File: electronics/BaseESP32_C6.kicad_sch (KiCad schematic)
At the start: 14 parts, among them P4 CONN_01X09, SW1 SW_Push, U1 ESP32-C6-MINI-1/U

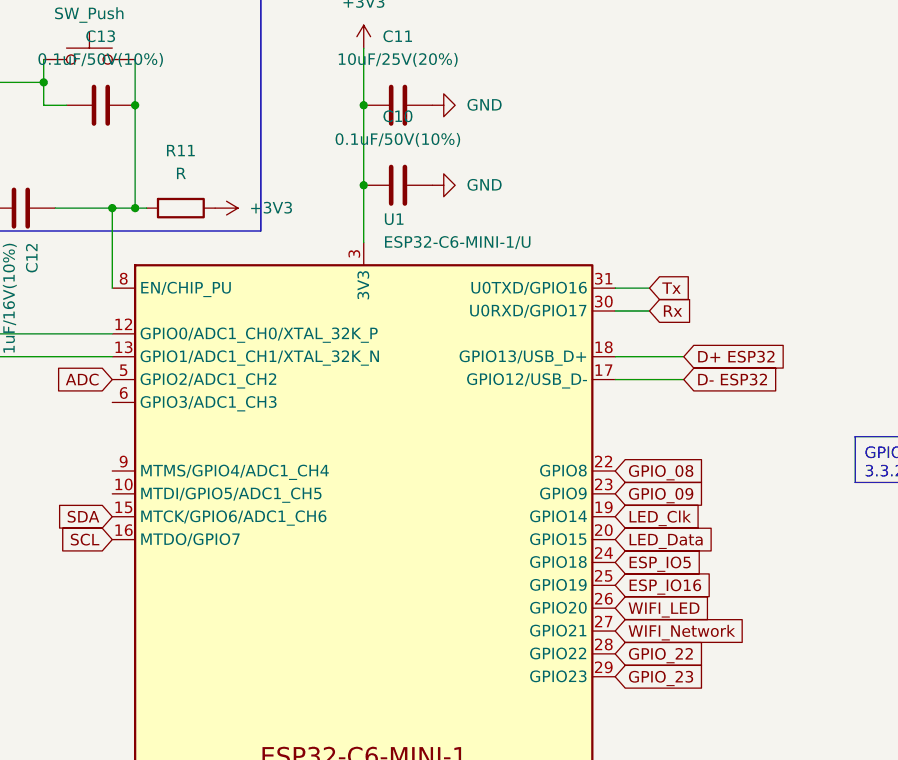
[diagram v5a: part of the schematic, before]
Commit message: Tidied tracks, added keepouts for ESP. Parts sourced except leds and small caps
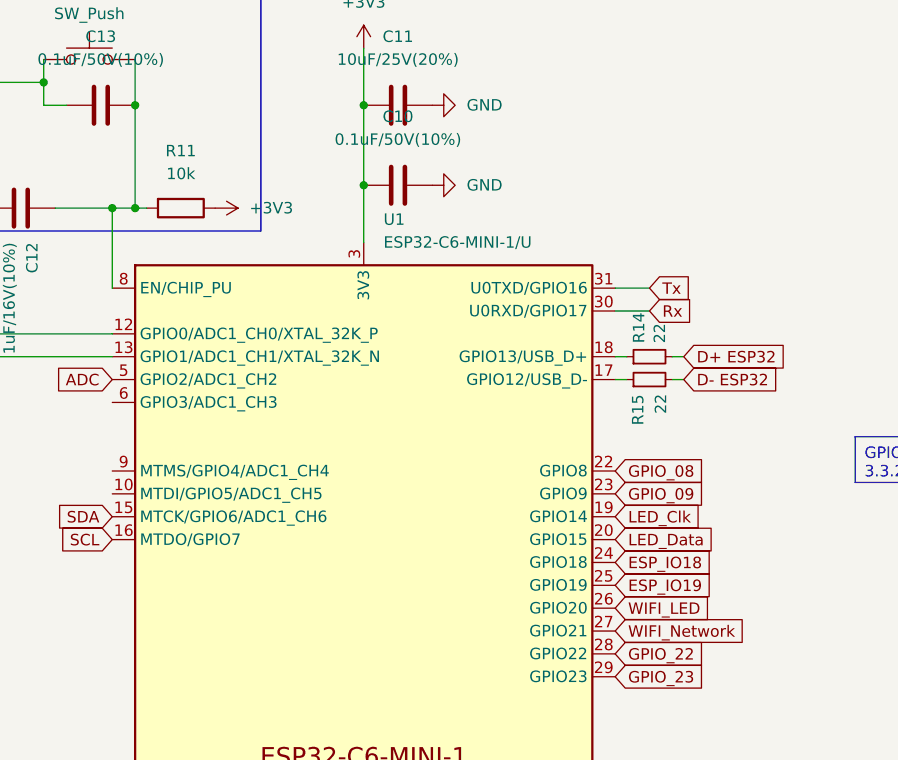
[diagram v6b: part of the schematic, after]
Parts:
- added R14, R15: 22, Resistor_SMD:R_0603_1608Metric_Pad0.98x0.95mm_HandSolder, symbol Device:R_Small
- R11: value R -> 10k; LCSC (none) -> C862388; LCSC Stock (none) -> https://www.lcsc.com/product-detail/Chip-span-style-backgro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
- R12, R13: LCSC (none) -> C5455512; LCSC Stock (none) -> https://www.lcsc.com/product-detail/Chip-span-style-backgro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
- U1: LCSC (none) -> C5736265; LCSC Stock (none) -> https://www.lcsc.com/product-detail/WiFi-Modules_Espressif-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
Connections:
- net D+ ESP32: now also R14.2; no longer U1.18 (GPIO13/USB_D+)
- net D- ESP32: now also R15.2; no longer U1.17 (GPIO12/USB_D-)
- net ESP_IO16 renamed ESP_IO19
- net ESP_IO5 renamed ESP_IO18
- new net: R14.1, U1.18 (GPIO13/USB_D+)
- new net: R15.1, U1.17 (GPIO12/USB_D-)
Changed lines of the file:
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@@
+    (stroke (width 0) (type default))
+  )
+  (wire (pts (xy 204.47 88.9) (xy 205.74 88.9))
     (stroke (width 0) (type default))
   )
@@
     (stroke (width 0) (type default))
   )
-  (wire (pts (xy 198.12 88.9) (xy 205.74 88.9))
-    (stroke (width 0) (type default))
-  )
   (wire (pts (xy 250.19 151.13) (xy 255.27 151.13))
     (stroke (width 0) (type default))
   )
+  (wire (pts (xy 198.12 88.9) (xy 199.39 88.9))
+    (stroke (width 0) (type default))
+  )
   (wire (pts (xy 134.62 60.96) (xy 134.62 58.42))
     (stroke (width 0) (type default))
@@
     (stroke (width 0) (type default))
   )
+  (wire (pts (xy 198.12 91.44) (xy 199.39 91.44))
+    (stroke (width 0) (type default))
+  )
   (wire (pts (xy 119.38 86.36) (xy 142.24 86.36))
     (stroke (width 0) (type default))
@@
     (stroke (width 0) (type default))
   )
-  (wire (pts (xy 198.12 91.44) (xy 205.74 91.44))
-    (stroke (width 0) (type default))
-  )
   (wire (pts (xy 135.89 72.39) (xy 142.24 72.39))
+    (stroke (width 0) (type default))
+  )
+  (wire (pts (xy 204.47 91.44) (xy 205.74 91.44))
     (stroke (width 0) (type default))
   )
@@
     )
   )
-  (global_label "ESP_IO5" (shape input) (at 198.12 111.76 0) (fields_autoplaced)
-    (effects (font (size 1.27 1.27)) (justify left))
-    (property "Intersheetrefs" "${INTERSHEET_REFS}" (at 207.9537 111.76 0)
+  (global_label "ESP_IO18" (shape input) (at 198.12 111.76 0) (fields_autoplaced)
+    (effects (font (size 1.27 1.27)) (justify left))
+    (property "Intersheetrefs" "${INTERSHEET_REFS}" (at 209.4014 111.76 0)
       (effects (font (size 1.27 1.27)) (justify left) hide)
     )
@@
     )
   )
-  (global_label "ESP_IO16" (shape input) (at 198.12 114.3 0) (fields_autoplaced)
-    (effects (font (size 1.27 1.27)) (justify left))
-    (property "Intersheetrefs" "${INTERSHEET_REFS}" (at 209.1632 114.3 0)
+  (global_label "ESP_IO19" (shape input) (at 198.12 114.3 0) (fields_autoplaced)
+    (effects (font (size 1.27 1.27)) (justify left))
+    (property "Intersheetrefs" "${INTERSHEET_REFS}" (at 209.4014 114.3 0)
       (effects (font (size 1.27 1.27)) (justify left) hide)
     )
@@
     )
   )
+  (symbol (lib_id "Device:R_Small") (at 201.93 88.9 90) (unit 1)
+    (in_bom yes) (on_board yes) (dnp no)
+    (property "Reference" "R14" (at 200.7616 87.4014 0)
+      (effects (font (size 1.27 1.27)) (justify left))
+    )
+    (property "Value" "22" (at 203.073 87.4014 0)
+      (effects (font (size 1.27 1.27)) (justify left))
+    )
+    (property "Footprint" "Resistor_SMD:R_0603_1608Metric_Pad0.98x0.95mm_HandSolder" (at 201.93 88.9 0)
+      (effects (font (size 1.27 1.27)) hide)
+    )
+    (property "Datasheet" "~" (at 201.93 88.9 0)
+      (effects (font (size 1.27 1.27)) hide)
+    )
+    (property "Farnell" "3495168 " (at 201.93 88.9 0)
+      (effects (font (size 1.27 1.27)) hide)
+    )
+    (property "Farnell Price/Stock" "https://uk.farnell.com/yageo/ac0201fr-0722rl/res-22r-1-0-05w-0201-thick-film/dp/3495168" (at 201.93 88.9 0)
+      (effects (font (size 1.27 1.27)) hide)
+    )
+    (property "LCSC" "C860239" (at 201.93 88.9 0)
+      (effects (font (size 1.27 1.27)) hide)
+    )
+    (property "LCSC Stock" "https://www.lcsc.com/product-detail/Chip-span-style-background-color-ff0-Resistor-span-Surface-Mount_YAGEO-RT0603BRB0722RL_C860239.html" (at 201.93 88.9 0)
+      (effects (font (size 1.27 1.27)) hide)
+    )
+    (pin "1")
+    (pin "2")
+    (instances
+      (project "MyBikesGotLED"
+        (path "/ea56fda8-6f8e-4826-a040-5c9b3e8e5cfa/88a3a1ef-5bc6-4f24-9217-01fd214eb76a"
+          (reference "R14") (unit 1)
+        )
+      )
+    )
+  )
   (symbol (lib_id "Connector:TestPoint") (at 119.38 86.36 90) (unit 1)
     (in_bom yes) (on_board yes) (dnp no)
@@
       (effects (font (size 1.27 1.27)) hide)
     )
+    (property "LCSC" "C5455512" (at 261.62 147.32 90)
+      (effects (font (size 1.27 1.27)) hide)
+    )
+    (property "LCSC Stock" "https://www.lcsc.com/product-detail/Chip-span-style-background-color-ff0-Resistor-span-Surface-Mount_YAGEO-AT0603BRD07560RL_C5455512.html" (at 261.62 147.32 90)
+      (effects (font (size 1.27 1.27)) hide)
+    )
     (pin "1")
     (pin "2")
@@
       (effects (font (size 1.27 1.27)) hide)
     )
+    (property "LCSC" "C5455512" (at 250.19 147.32 90)
+      (effects (font (size 1.27 1.27)) hide)
+    )
+    (property "LCSC Stock" "https://www.lcsc.com/product-detail/Chip-span-style-background-color-ff0-Resistor-span-Surface-Mount_YAGEO-AT0603BRD07560RL_C5455512.html" (at 250.19 147.32 90)
+      (effects (font (size 1.27 1.27)) hide)
+    )
     (pin "1")
     (pin "2")
@@
     )
   )
+  (symbol (lib_id "Device:R_Small") (at 201.93 91.44 90) (unit 1)
+    (in_bom yes) (on_board yes) (dnp no)
+    (property "Reference" "R15" (at 200.66 96.52 0)
+      (effects (font (size 1.27 1.27)) (justify left))
+    )
+    (property "Value" "22" (at 203.2 95.25 0)
+      (effects (font (size 1.27 1.27)) (justify left))
+    )
+    (property "Footprint" "Resistor_SMD:R_0603_1608Metric_Pad0.98x0.95mm_HandSolder" (at 201.93 91.44 0)
+      (effects (font (size 1.27 1.27)) hide)
+    )
+    (property "Datasheet" "~" (at 201.93 91.44 0)
+      (effects (font (size 1.27 1.27)) hide)
+    )
+    (property "Farnell" "3495168 " (at 201.93 91.44 0)
+      (effects (font (size 1.27 1.27)) hide)
+    )
+    (property "Farnell Price/Stock" "https://uk.farnell.com/yageo/ac0201fr-0722rl/res-22r-1-0-05w-0201-thick-film/dp/3495168" (at 201.93 91.44 0)
+      (effects (font (size 1.27 1.27)) hide)
+    )
+    (property "LCSC" "C860239" (at 201.93 91.44 0)
+      (effects (font (size 1.27 1.27)) hide)
+    )
+    (property "LCSC Stock" "https://www.lcsc.com/product-detail/Chip-span-style-background-color-ff0-Resistor-span-Surface-Mount_YAGEO-RT0603BRB0722RL_C860239.html" (at 201.93 91.44 0)
+      (effects (font (size 1.27 1.27)) hide)
+    )
+    (pin "1")
+    (pin "2")
+    (instances
+      (project "MyBikesGotLED"
+        (path "/ea56fda8-6f8e-4826-a040-5c9b3e8e5cfa/88a3a1ef-5bc6-4f24-9217-01fd214eb76a"
+          (reference "R15") (unit 1)
+        )
+      )
+    )
+  )
   (symbol (lib_id "power:GND") (at 68.58 33.02 180) (unit 1)
     (in_bom yes) (on_board yes) (dnp no)
@@
       (effects (font (size 1.27 1.27)))
     )
-    (property "Value" "R" (at 149.86 68.58 90)
+    (property "Value" "10k" (at 149.86 68.58 90)
       (effects (font (size 1.27 1.27)))
     )
@@
     )
     (property "Datasheet" "~" (at 149.86 72.39 0)
+      (effects (font (size 1.27 1.27)) hide)
+    )
+    (property "LCSC" "C862388" (at 149.86 72.39 90)
+      (effects (font (size 1.27 1.27)) hide)
+    )
+    (property "LCSC Stock" "https://www.lcsc.com/product-detail/Chip-span-style-background-color-ff0-Resistor-span-Surface-Mount_YAGEO-RT0603CRD0710KL_C862388.html" (at 149.86 72.39 90)
       (effects (font (size 1.27 1.27)) hide)
     )
@@
       (effects (font (size 1.27 1.27)) hide)
     )
+    (property "LCSC" "C5736265" (at 170.18 109.22 0)
+      (effects (font (size 1.27 1.27)) hide)
+    )
+    (property "LCSC Stock" "https://www.lcsc.com/product-detail/WiFi-Modules_Espressif-Systems-ESP32-C6-MINI-1-N4_C5736265.html" (at 170.18 109.22 0)
+      (effects (font (size 1.27 1.27)) hide)
+    )

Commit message: /production added with all LCSC stock in BOM
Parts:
- C10, C13: LCSC (none) -> C237171; LCSC Stock (none) -> https://www.lcsc.com/product-detail/Multilayer-Ceramic-Capa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
- C11: LCSC (none) -> C76614; LCSC Stock (none) -> https://www.lcsc.com/product-detail/Multilayer-Ceramic-Capa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
- C12: LCSC (none) -> C85862; LCSC Stock (none) -> https://www.lcsc.com/product-detail/Multilayer-Ceramic-Capa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
- D5: LCSC (none) -> C497949; LCSC Stock (none) -> https://www.lcsc.com/product-detail/LED-Indication-Discrete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
- D6: LCSC (none) -> C497935; LCSC Stock (none) -> https://www.lcsc.com/product-detail/LED-Indication-Discrete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
- SW1: LCSC (none) -> C221772; LCSC Stock (none) -> https://www.lcsc.com/product-detail/Tactile-Switches_C-K-KS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
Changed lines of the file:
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@@
+      (effects (font (size 1.27 1.27)) hide)
+    )
+    (property "LCSC" "C85862" (at 132.08 72.39 0)
+      (effects (font (size 1.27 1.27)) hide)
+    )
+    (property "LCSC Stock" "https://www.lcsc.com/product-detail/Multilayer-Ceramic-Capacitors-MLCC-SMD-SMT_Murata-Electronics-GCM188R71E105KA64D_C85862.html" (at 132.08 72.39 0)
       (effects (font (size 1.27 1.27)) hide)
     )
@@
       (effects (font (size 1.27 1.27)) hide)
     )
+    (property "LCSC" "C497949" (at 261.62 137.16 0)
+      (effects (font (size 1.27 1.27)) hide)
+    )
+    (property "LCSC Stock" "https://www.lcsc.com/product-detail/LED-Indication-Discrete_HONGLITRONIC-Hongli-Zhihui-HONGLITRONIC-HL-PSC-2012U36FC_C497949.html" (at 261.62 137.16 0)
+      (effects (font (size 1.27 1.27)) hide)
+    )
     (pin "1")
     (pin "2")
@@
       (effects (font (size 1.27 1.27)) hide)
     )
+    (property "LCSC" "C221772" (at 139.7 55.88 0)
+      (effects (font (size 1.27 1.27)) hide)
+    )
+    (property "LCSC Stock" "https://www.lcsc.com/product-detail/Tactile-Switches_C-K-KSEK43GLFS_C221772.html" (at 139.7 55.88 0)
+      (effects (font (size 1.27 1.27)) hide)
+    )
     (pin "2")
     (pin "1")
@@
     )
     (property "Datasheet" "~" (at 140.97 60.96 0)
+      (effects (font (size 1.27 1.27)) hide)
+    )
+    (property "LCSC" "C237171" (at 140.97 60.96 90)
+      (effects (font (size 1.27 1.27)) hide)
+    )
+    (property "LCSC Stock" "https://www.lcsc.com/product-detail/Multilayer-Ceramic-Capacitors-MLCC-SMD-SMT_Walsin-Tech-Corp-0603B104J250CT_C237171.html" (at 140.97 60.96 90)
       (effects (font (size 1.27 1.27)) hide)
     )
@@
       (effects (font (size 1.27 1.27)) hide)
     )
+    (property "LCSC" "C497935" (at 250.19 137.16 0)
+      (effects (font (size 1.27 1.27)) hide)
+    )
+    (property "LCSC Stock" "https://www.lcsc.com/product-detail/LED-Indication-Discrete_HONGLITRONIC-Hongli-Zhihui-HONGLITRONIC-HL-PST-1608S22OC-04_C497935.html" (at 250.19 137.16 0)
+      (effects (font (size 1.27 1.27)) hide)
+    )
     (pin "1")
     (pin "2")
@@
       (effects (font (size 1.27 1.27)) hide)
     )
+    (property "LCSC" "C237171" (at 173.99 69.85 90)
+      (effects (font (size 1.27 1.27)) hide)
+    )
+    (property "LCSC Stock" "https://www.lcsc.com/product-detail/Multilayer-Ceramic-Capacitors-MLCC-SMD-SMT_Walsin-Tech-Corp-0603B104J250CT_C237171.html" (at 173.99 69.85 90)
+      (effects (font (size 1.27 1.27)) hide)
+    )
     (pin "2")
     (pin "1")
@@
       (effects (font (size 1.27 1.27)) hide)
     )
+    (property "LCSC" "C76614" (at 173.99 60.96 90)
+      (effects (font (size 1.27 1.27)) hide)
+    )
+    (property "LCSC Stock" "https://www.lcsc.com/product-detail/Multilayer-Ceramic-Capacitors-MLCC-SMD-SMT_TDK-C1608X5R1E106MT000E_C76614.html" (at 173.99 60.96 90)
+      (effects (font (size 1.27 1.27)) hide)
+    )

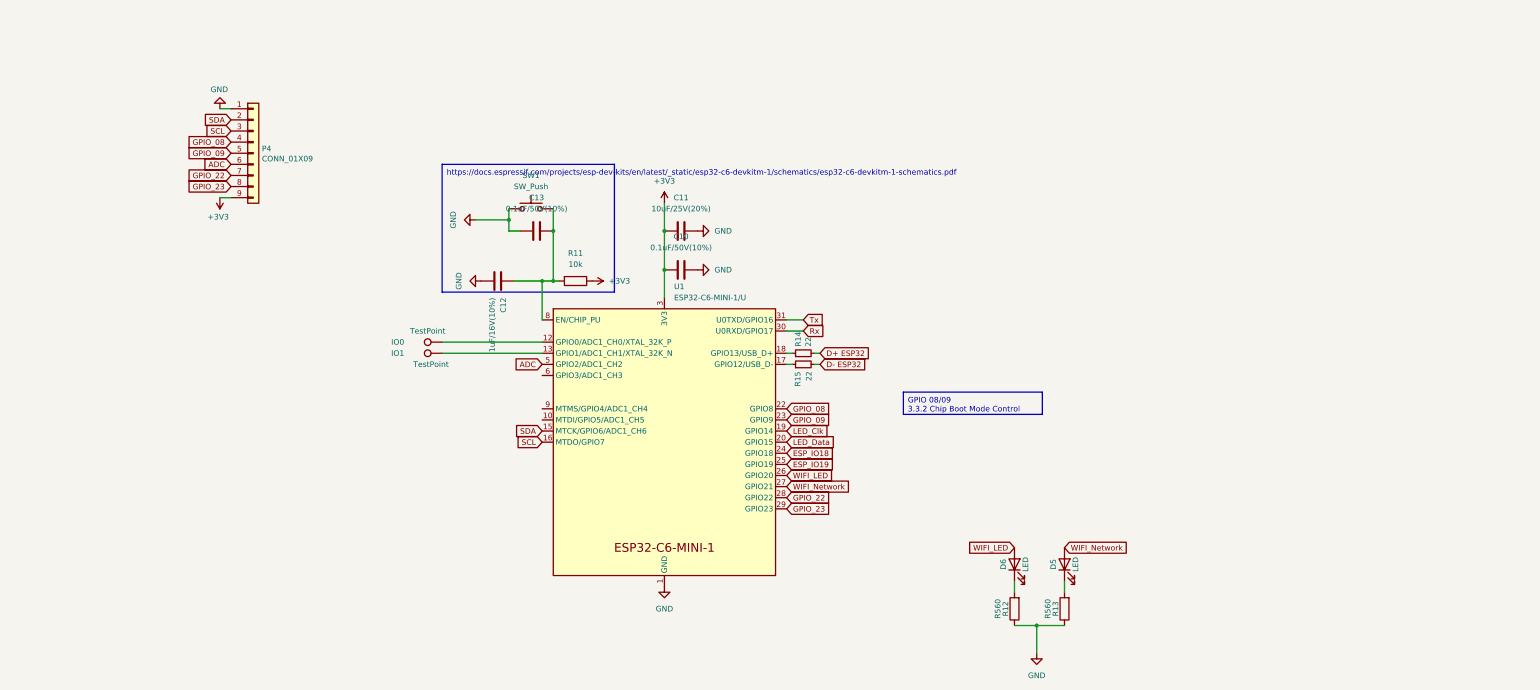
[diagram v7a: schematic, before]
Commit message: Add boot pins, replace usb
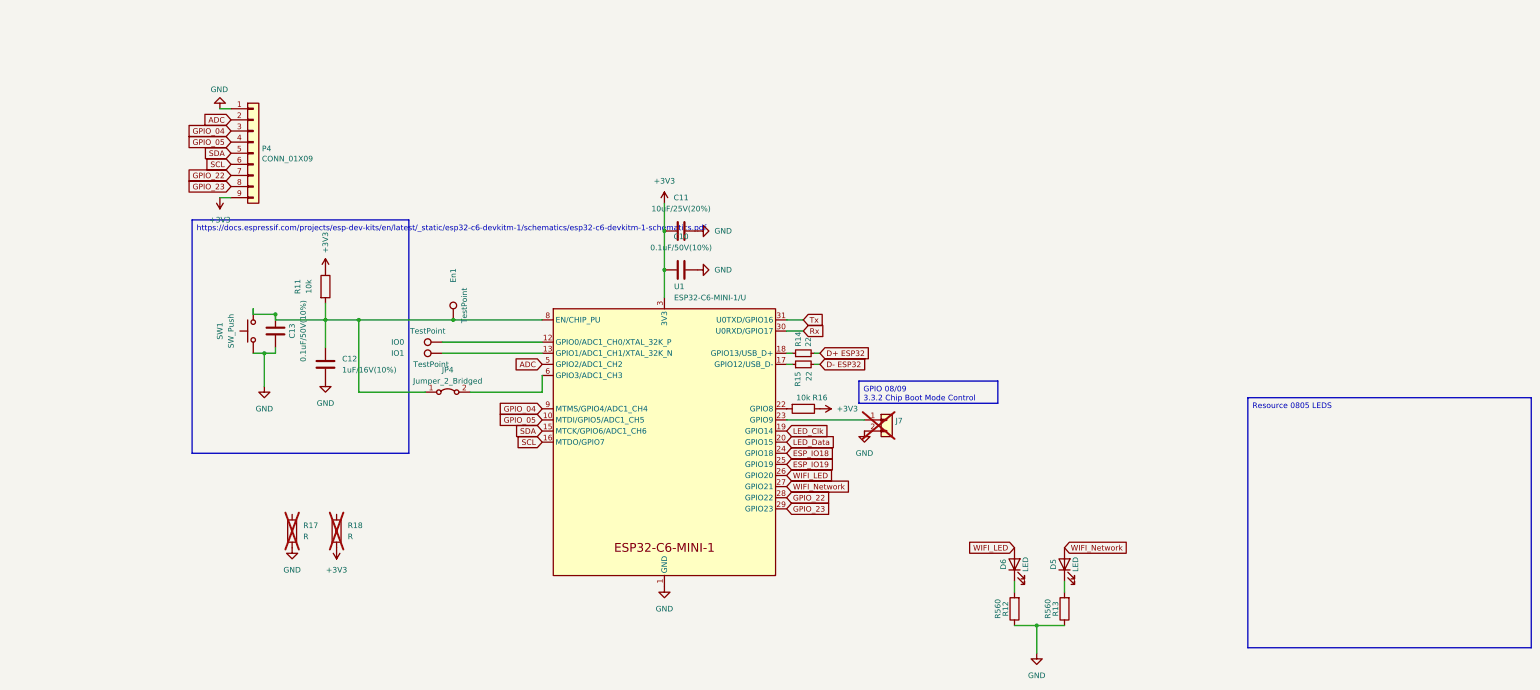
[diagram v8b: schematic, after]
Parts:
- added En1: TestPoint, TestPoint:TestPoint_Pad_D2.5mm, symbol Connector:TestPoint
- added J7: Battery_Test_Points, Connector_PinSocket_2.54mm:PinSocket_1x02_P2.54mm_Vertical, symbol Connector_Generic:Conn_01x02
- added JP4: Jumper_2_Bridged, Jumper:SolderJumper-2_P1.3mm_Bridged_RoundedPad1.0x1.5mm, symbol Jumper:Jumper_2_Bridged
- added R16: 10k, Resistor_SMD:R_0603_1608Metric_Pad0.98x0.95mm_HandSolder, symbol Device:R
- added R17, R18: R, Resistor_SMD:R_0805_2012Metric, symbol Device:R
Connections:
- net +3V3: now also R16.1, R18.2
- net ADC: now also P4.2 (Pin_2); no longer P4.6 (Pin_6)
- net GND: now also J7.2 (Pin_2), R17.2
- net SCL: now also P4.6 (Pin_6); no longer P4.3 (Pin_3)
- net SDA: now also P4.5 (Pin_5); no longer P4.2 (Pin_2)
- net at C12.1, C13.1, R11.2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: now also En1.1, JP4.1 (A)
- net GPIO_05: now reaches U1.10 (MTDI/GPIO5/ADC1_CH5)
- net GPIO_05: now also P4.4 (Pin_4)
- net at U1.6 (GPIO3/ADC1_CH3): now also JP4.2 (B)
- net GPIO_04: now reaches U1.9 (MTMS/GPIO4/ADC1_CH4)
- net GPIO_04: now also P4.3 (Pin_3)
- net GPIO_08: no longer names the net of U1.22 (GPIO8)
- net GPIO_08: now also R16.2; no longer P4.4 (Pin_4)
- net GPIO_09: no longer names the net of U1.23 (GPIO9)
- net GPIO_09: now also J7.1 (Pin_1); no longer P4.5 (Pin_5)
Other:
- moved on the sheet: C12, C13, R11, SW1
